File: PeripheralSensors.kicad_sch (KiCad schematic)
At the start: 14 parts, among them J19 TOF_Connectors, J21 IMU_Conn, U2 SAM-M8Q

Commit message: after connor fixed footprints and billy started layout
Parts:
- C12: footprint CustomComponents:CAPC1608X90N_ -> LocalComponents:CAPC1608X90N_
- D6: footprint CustomComponents:LED_LTST-C171_LTO -> LocalComponents:LED_LTST-C171_LTO
- R24: footprint CustomComponents:RESC1508X55N -> LocalComponents:RESC1508X55N
- R28, R9: footprint CustomComponents:RESC6332X65N -> LocalComponents:RESC6332X65N
- R29, R30: footprint CustomComponents:R0402 -> LocalComponents:R0402
- R31, R32: footprint CustomComponents:RESC1005X35N -> LocalComponents:RESC1005X35N
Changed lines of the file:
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@@
 			)
 		)
-		(property "Footprint" "CustomComponents:R0402"
+		(property "Footprint" "LocalComponents:R0402"
 			(at 92.71 64.008 90)
 			(effects
@@
 			)
 		)
-		(property "Footprint" "CustomComponents:RESC6332X65N"
+		(property "Footprint" "LocalComponents:RESC6332X65N"
 			(at 88.9 50.038 90)
 			(effects
@@
 			)
 		)
-		(property "Footprint" "CustomComponents:CAPC1608X90N_"
+		(property "Footprint" "LocalComponents:CAPC1608X90N_"
 			(at 83.82 35.8648 0)
 			(effects
@@
 			)
 		)
-		(property "Footprint" "CustomComponents:RESC1005X35N"
+		(property "Footprint" "LocalComponents:RESC1005X35N"
 			(at 106.172 69.85 90)
 			(effects
@@
 			)
 		)
-		(property "Footprint" "CustomComponents:RESC1005X35N"
+		(property "Footprint" "LocalComponents:RESC1005X35N"
 			(at 96.012 69.85 90)
 			(effects
@@
 			)
 		)
-		(property "Footprint" "CustomComponents:RESC6332X65N"
+		(property "Footprint" "LocalComponents:RESC6332X65N"
 			(at 88.9 49.022 90)
 			(effects
@@
 			)
 		)
-		(property "Footprint" "CustomComponents:LED_LTST-C171_LTO"
+		(property "Footprint" "LocalComponents:LED_LTST-C171_LTO"
 			(at 35.56 67.31 0)
 			(effects
@@
 			)
 		)
-		(property "Footprint" "CustomComponents:R0402"
+		(property "Footprint" "LocalComponents:R0402"
 			(at 92.71 62.992 90)
 			(effects
@@
 			)
 		)
-		(property "Footprint" "CustomComponents:RESC1508X55N"
+		(property "Footprint" "LocalComponents:RESC1508X55N"
 			(at 37.338 58.42 90)
 			(effects

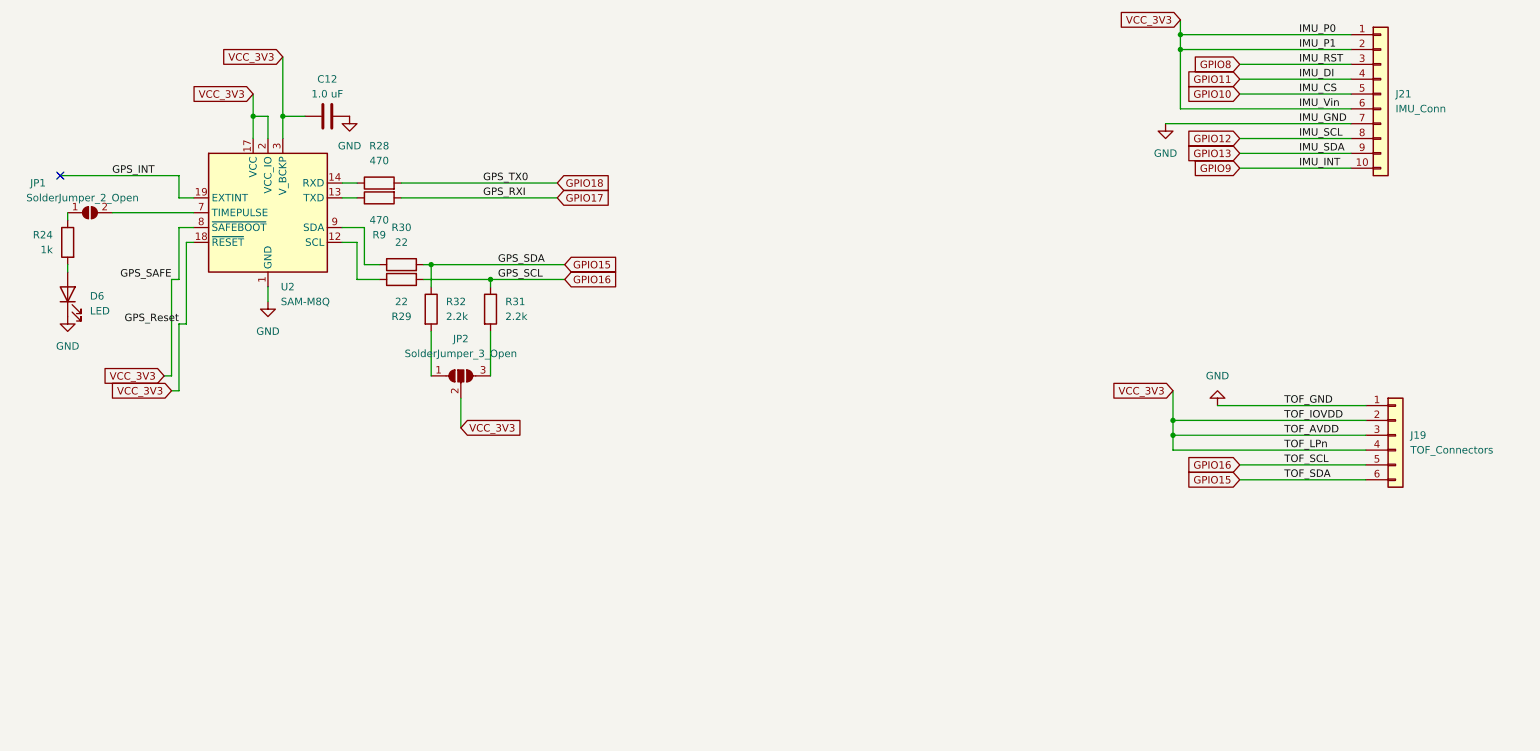
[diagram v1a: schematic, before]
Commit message: added esd to imu and tof
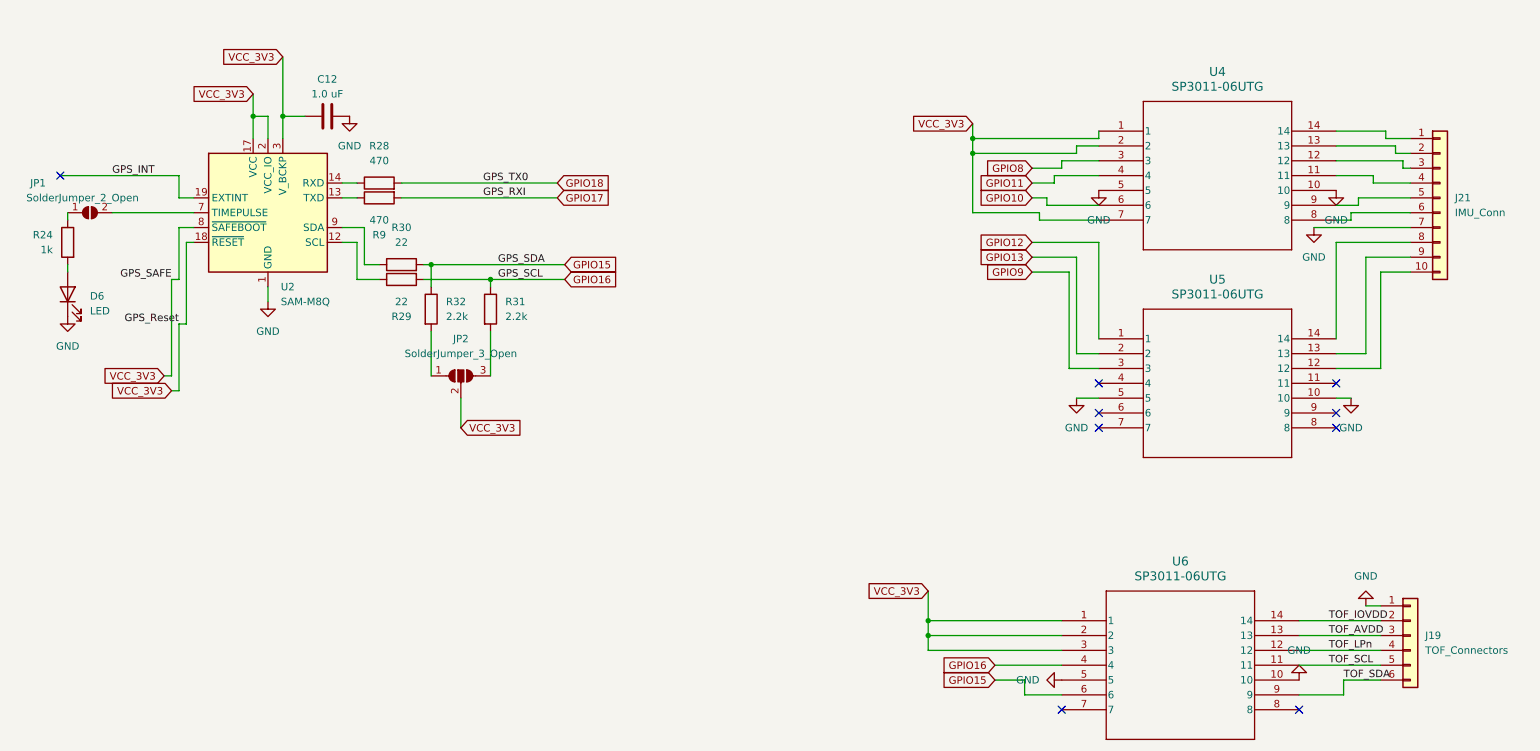
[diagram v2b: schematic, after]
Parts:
- added U4, U5, U6: SP3011-06UTG, LocalComponents:SON14_SP3011-06UTG_LTF, symbol LocalComps:SP3011-06UTG
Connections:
- net GND: now also U4.10, U4.5, U5.10, U5.5, U6.10, U6.5
- net GPIO10: now also U4.6; no longer J21.5 (Pin_5)
- net GPIO11: now also U4.4; no longer J21.4 (Pin_4)
- net GPIO12: now also U5.1; no longer J21.8 (Pin_8)
- net GPIO13: now also U5.2; no longer J21.9 (Pin_9)
- net GPIO15: now also U6.6; no longer J19.6 (Pin_6)
- net GPIO16: now also U6.4; no longer J19.5 (Pin_5)
- net GPIO8: now also U4.3; no longer J21.3 (Pin_3)
- net GPIO9: now also U5.3; no longer J21.10 (Pin_10)
- net VCC_3V3: now also U4.1, U4.2, U4.7, U6.1, U6.2, U6.3; no longer J19.2 (Pin_2), J19.3 (Pin_3), J19.4 (Pin_4), J21.1 (Pin_1), J21.2 (Pin_2), J21.6 (Pin_6)
- new net: J21.4 (Pin_4), U4.11
- new net: J21.3 (Pin_3), U4.12
- new net: J21.2 (Pin_2), U4.13
- new net: J21.1 (Pin_1), U4.14
- new net: J21.6 (Pin_6), U4.8
- new net: J21.5 (Pin_5), U4.9
- new net: J21.10 (Pin_10), U5.12
- new net: J21.9 (Pin_9), U5.13
- new net: J21.8 (Pin_8), U5.14
- new net TOF_AVDD: J19.3 (Pin_3), U6.13
- new net TOF_IOVDD: J19.2 (Pin_2), U6.14
- new net TOF_LPn: J19.4 (Pin_4), U6.12
- new net TOF_SCL: J19.5 (Pin_5), U6.11
- new net TOF_SDA: J19.6 (Pin_6), U6.9
- no-connect marks 1 -> 9
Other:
- moved on the sheet: J19, J21

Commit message: pcb draft 2 from billy
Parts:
- removed U4, U5, U6: SP3011-06UTG, LocalComponents:SON14_SP3011-06UTG_LTF, symbol LocalComps:SP3011-06UTG
- added D1, D2: ESDS304, Package_TO_SOT_SMD:SOT-23-5, symbol Power_Protection:ESDS304
- added U4, U5: SP3011-06UTG, LocalComponents:SON14_SP3011-06UTG_LTF, symbol Custom_Components:SP3011-06UTG
- D6: footprint LocalComponents:LED_LTST-C171_LTO -> LED_SMD:LED_0201_0603Metric
- R24: footprint LocalComponents:RESC1508X55N -> Resistor_SMD:R_0805_2012Metric_Pad1.20x1.40mm_HandSolder
- R28, R9: footprint LocalComponents:RESC6332X65N -> Resistor_SMD:R_0805_2012Metric_Pad1.20x1.40mm_HandSolder
- R29, R30: footprint LocalComponents:R0402 -> Resistor_SMD:R_0805_2012Metric_Pad1.20x1.40mm_HandSolder
- R31, R32: footprint LocalComponents:RESC1005X35N -> Resistor_SMD:R_0805_2012Metric_Pad1.20x1.40mm_HandSolder
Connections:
- net TOF_AVDD is gone; now on net VCC_3V3: J19.3 (Pin_3)
- net TOF_IOVDD is gone; now on net VCC_3V3: J19.2 (Pin_2)
- net TOF_LPn is gone; now on net VCC_3V3: J19.4 (Pin_4)
- net GND: now also D1.2 (A), D2.2 (A), U4.10, U5.10
- net GPIO10: now also U4.3
- net GPIO11: now also U4.2
- net GPIO12: now also U4.4
- net GPIO13: now also U4.6
- net GPIO15: now also U5.2
- net GPIO16: now also U5.1
- net GPIO8: now also U4.1
- net GPIO9: now also U4.7
- net TOF_SCL: now also U5.14
- net TOF_SDA: now also U5.13
- net VCC_3V3: now also J21.1 (Pin_1), J21.2 (Pin_2), J21.6 (Pin_6), D1.1 (K), D1.3 (K), D1.4 (K), D2.1 (K), D2.3 (K), D2.4 (K)
- net IMU_DI: now reaches J21.4 (Pin_4)
- net IMU_DI: now also U4.13
- net IMU_RST: now reaches J21.3 (Pin_3)
- net IMU_RST: now also U4.14
- net IMU_CS: now reaches J21.5 (Pin_5)
- net IMU_CS: now also U4.12
- net IMU_INT: now reaches J21.10 (Pin_10)
- net IMU_INT: now also U4.8
- net IMU_SDA: now reaches J21.9 (Pin_9)
- net IMU_SDA: now also U4.9
- net IMU_SCL: now reaches J21.8 (Pin_8)
- net IMU_SCL: now also U4.11
- no-connect marks 9 -> 13
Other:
- moved on the sheet: J19, J21
